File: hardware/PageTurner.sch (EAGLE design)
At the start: 11 parts

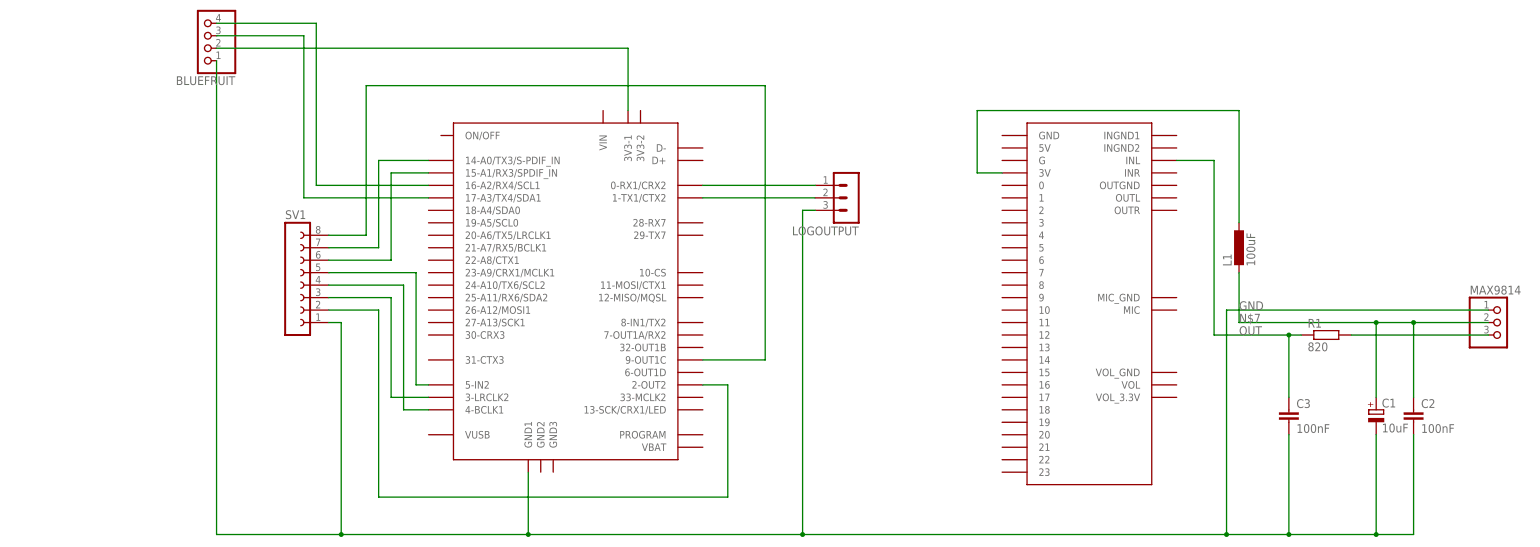
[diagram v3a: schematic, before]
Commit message: trained new model and made python programm not crashing if teensy connection breaks
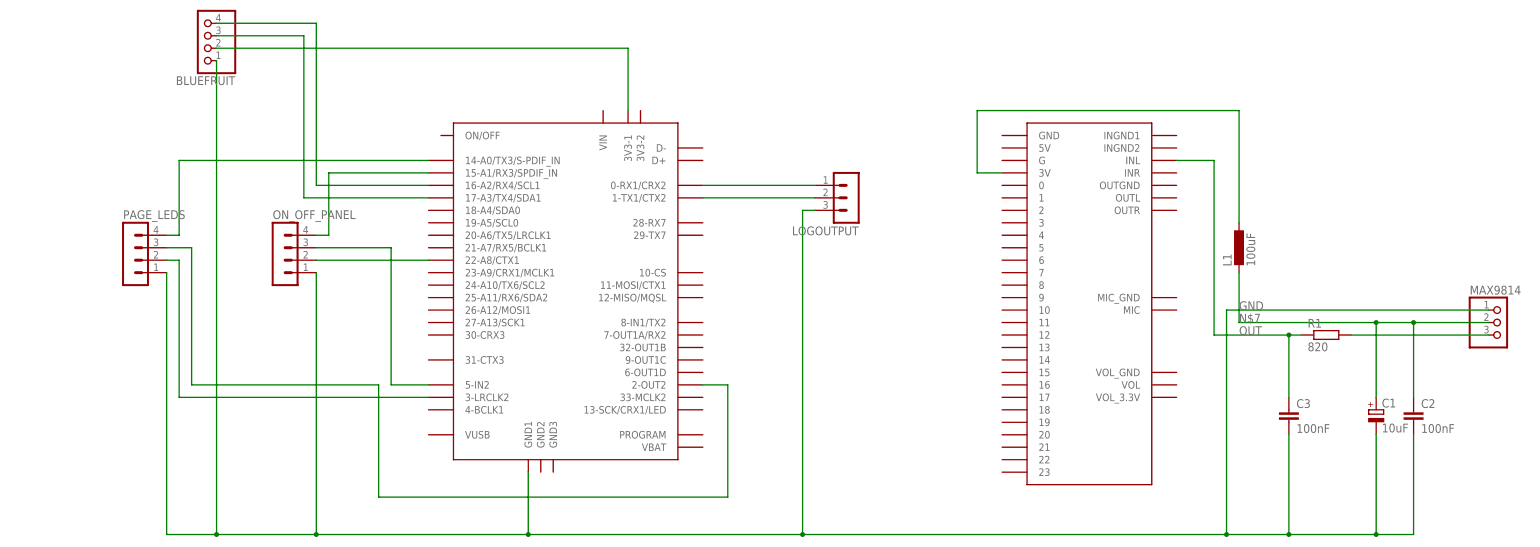
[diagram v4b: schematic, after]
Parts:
- removed SV1: (no value), con-lsta:FE08-1
- added ON_OFF_PANEL, PAGE_LEDS: (no value), con-lstb:MA04-1
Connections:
- net N$10 renamed LOG_TX
- net N$8 renamed LOG_RX
- removed net N$11: SV1.5, U$1.5-IN2
- removed net N$12: SV1.6, U$1.15-A1/RX3/SPDIF_IN
- removed net N$9: SV1.4, U$1.4-BCLK1
- new net N$8: PAGE_LEDS.2, U$1.3-LRCLK2
- net GND: now also ON_OFF_PANEL.1, PAGE_LEDS.1; no longer SV1.1
- net N$1: now also PAGE_LEDS.3; no longer SV1.2
- net N$2: now also PAGE_LEDS.4, U$1.14-A0/TX3/S-PDIF_IN; no longer SV1.7
- net N$3: now also ON_OFF_PANEL.4, U$1.15-A1/RX3/SPDIF_IN; no longer SV1.8, U$1.9-OUT1C
- net N$5: now also ON_OFF_PANEL.3, U$1.5-IN2; no longer U$1.14-A0/TX3/S-PDIF_IN
- net N$6: now also ON_OFF_PANEL.2, U$1.22-A8/CTX1; no longer SV1.3, U$1.3-LRCLK2
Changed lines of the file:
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@@
 <part name="MAX9814" library="pinhead" library_urn="urn:adsk.eagle:library:325" deviceset="PINHD-1X3" device="" package3d_urn="urn:adsk.eagle:package:22458/2"/>
 <part name="BLUEFRUIT" library="pinhead" library_urn="urn:adsk.eagle:library:325" deviceset="PINHD-1X4" device="" package3d_urn="urn:adsk.eagle:package:22407/2"/>
-<part name="SV1" library="con-lsta" library_urn="urn:adsk.eagle:library:161" deviceset="FE08-1" device="" package3d_urn="urn:adsk.eagle:package:8194/1"/>
 <part name="R1" library="rcl" library_urn="urn:adsk.eagle:library:334" deviceset="R-EU_" device="0207/7" package3d_urn="urn:adsk.eagle:package:23493/2" value="820"/>
 <part name="C1" library="rcl" library_urn="urn:adsk.eagle:library:334" deviceset="CPOL-EU" device="E2-4" package3d_urn="urn:adsk.eagle:package:23347/1" value="10uF"/>
@@
 <part name="L1" library="rcl" library_urn="urn:adsk.eagle:library:334" deviceset="L-EU" device="0207/5V" package3d_urn="urn:adsk.eagle:package:23502/1" value="100uF"/>
 <part name="C3" library="rcl" library_urn="urn:adsk.eagle:library:334" deviceset="C-EU" device="025-040X050" package3d_urn="urn:adsk.eagle:package:23634/1" value="100nF"/>
+<part name="PAGE_LEDS" library="con-lstb" library_urn="urn:adsk.eagle:library:162" deviceset="MA04-1" device="" package3d_urn="urn:adsk.eagle:package:8337/1"/>
+<part name="ON_OFF_PANEL" library="con-lstb" library_urn="urn:adsk.eagle:library:162" deviceset="MA04-1" device="" package3d_urn="urn:adsk.eagle:package:8337/1"/>
 </parts>
 <sheets>
@@
 <attribute name="VALUE" x="-11.43" y="109.22" size="1.778" layer="96" rot="R180"/>
 </instance>
-<instance part="SV1" gate="G$1" x="0" y="50.8" smashed="yes">
-<attribute name="VALUE" x="-1.27" y="38.1" size="1.778" layer="96"/>
-<attribute name="NAME" x="-1.27" y="64.262" size="1.778" layer="95"/>
-</instance>
 <instance part="R1" gate="G$1" x="210.82" y="40.64" smashed="yes">
 <attribute name="NAME" x="207.01" y="42.1386" size="1.778" layer="95"/>
@@
 <attribute name="NAME" x="204.724" y="25.781" size="1.778" layer="95"/>
 <attribute name="VALUE" x="204.724" y="20.701" size="1.778" layer="96"/>
+</instance>
+<instance part="PAGE_LEDS" gate="1" x="-33.02" y="58.42" smashed="yes">
+<attribute name="VALUE" x="-34.29" y="48.26" size="1.778" layer="96"/>
+<attribute name="NAME" x="-34.29" y="64.262" size="1.778" layer="95"/>
+</instance>
+<instance part="ON_OFF_PANEL" gate="1" x="-2.54" y="58.42" smashed="yes">
+<attribute name="VALUE" x="-3.81" y="48.26" size="1.778" layer="96"/>
+<attribute name="NAME" x="-3.81" y="64.262" size="1.778" layer="95"/>
 </instance>
 </instances>
@@
 </busses>
 <nets>
-<net name="N$9" class="0">
-<segment>
-<pinref part="SV1" gate="G$1" pin="4"/>
-<wire x1="7.62" y1="50.8" x2="22.86" y2="50.8" width="0.1524" layer="91"/>
-<wire x1="22.86" y1="50.8" x2="22.86" y2="25.4" width="0.1524" layer="91"/>
-<pinref part="U$1" gate="G$1" pin="4-BCLK1"/>
-<wire x1="22.86" y1="25.4" x2="27.94" y2="25.4" width="0.1524" layer="91"/>
-</segment>
-</net>
-<net name="N$8" class="0">
+<net name="LOG_RX" class="0">
 <segment>
 <pinref part="U$1" gate="G$1" pin="0-RX1/CRX2"/>
@@
 </segment>
 </net>
-<net name="N$10" class="0">
+<net name="LOG_TX" class="0">
 <segment>
 <pinref part="U$1" gate="G$1" pin="1-TX1/CTX2"/>
@@
 <wire x1="88.9" y1="30.48" x2="88.9" y2="7.62" width="0.1524" layer="91"/>
 <wire x1="88.9" y1="7.62" x2="17.78" y2="7.62" width="0.1524" layer="91"/>
-<wire x1="17.78" y1="7.62" x2="17.78" y2="45.72" width="0.1524" layer="91"/>
-<pinref part="SV1" gate="G$1" pin="2"/>
-<wire x1="17.78" y1="45.72" x2="7.62" y2="45.72" width="0.1524" layer="91"/>
+<wire x1="17.78" y1="7.62" x2="17.78" y2="30.48" width="0.1524" layer="91"/>
+<pinref part="PAGE_LEDS" gate="1" pin="3"/>
+<wire x1="-25.4" y1="58.42" x2="-20.32" y2="58.42" width="0.1524" layer="91"/>
+<wire x1="-20.32" y1="58.42" x2="-20.32" y2="30.48" width="0.1524" layer="91"/>
+<wire x1="-20.32" y1="30.48" x2="17.78" y2="30.48" width="0.1524" layer="91"/>
 </segment>
 </net>
@@
 <wire x1="190.5" y1="45.72" x2="190.5" y2="0" width="0.1524" layer="91"/>
 <pinref part="U$1" gate="G$1" pin="GND1"/>
-<wire x1="-15.24" y1="0" x2="10.16" y2="0" width="0.1524" layer="91"/>
-<wire x1="10.16" y1="0" x2="48.26" y2="0" width="0.1524" layer="91"/>
+<wire x1="-15.24" y1="0" x2="5.08" y2="0" width="0.1524" layer="91"/>
+<wire x1="5.08" y1="0" x2="48.26" y2="0" width="0.1524" layer="91"/>
 <wire x1="48.26" y1="0" x2="48.26" y2="12.7" width="0.1524" layer="91"/>
 <pinref part="LOGOUTPUT" gate="G$1" pin="3"/>
@@
 <pinref part="BLUEFRUIT" gate="A" pin="1"/>
 <wire x1="-15.24" y1="96.52" x2="-15.24" y2="0" width="0.1524" layer="91"/>
-<pinref part="SV1" gate="G$1" pin="1"/>
-<wire x1="7.62" y1="43.18" x2="10.16" y2="43.18" width="0.1524" layer="91"/>
-<wire x1="10.16" y1="43.18" x2="10.16" y2="0" width="0.1524" layer="91"/>
-<junction x="10.16" y="0"/>
 <pinref part="C1" gate="G$1" pin="-"/>
 <wire x1="220.98" y1="20.32" x2="220.98" y2="0" width="0.1524" layer="91"/>
@@
 <wire x1="203.2" y1="20.32" x2="203.2" y2="0" width="0.1524" layer="91"/>
 <junction x="203.2" y="0"/>
+<pinref part="PAGE_LEDS" gate="1" pin="1"/>
+<wire x1="-25.4" y1="53.34" x2="-25.4" y2="0" width="0.1524" layer="91"/>
+<wire x1="-25.4" y1="0" x2="-15.24" y2="0" width="0.1524" layer="91"/>
+<junction x="-15.24" y="0"/>
+<pinref part="ON_OFF_PANEL" gate="1" pin="1"/>
+<wire x1="5.08" y1="53.34" x2="5.08" y2="0" width="0.1524" layer="91"/>
+<junction x="5.08" y="0"/>
 </segment>
 </net>
@@
 </segment>
 </net>
-<net name="N$3" class="0">
-<segment>
-<pinref part="U$1" gate="G$1" pin="9-OUT1C"/>
-<wire x1="96.52" y1="35.56" x2="83.82" y2="35.56" width="0.1524" layer="91"/>
-<pinref part="SV1" gate="G$1" pin="8"/>
-<wire x1="7.62" y1="60.96" x2="15.24" y2="60.96" width="0.1524" layer="91"/>
-<wire x1="15.24" y1="60.96" x2="15.24" y2="91.44" width="0.1524" layer="91"/>
-<wire x1="15.24" y1="91.44" x2="96.52" y2="91.44" width="0.1524" layer="91"/>
-<wire x1="96.52" y1="91.44" x2="96.52" y2="35.56" width="0.1524" layer="91"/>
-</segment>
-</net>
 <net name="BLE_TX" class="0">
 <segment>
@@
 </segment>
 </net>
-<net name="N$6" class="0">
-<segment>
-<pinref part="SV1" gate="G$1" pin="3"/>
-<wire x1="7.62" y1="48.26" x2="20.32" y2="48.26" width="0.1524" layer="91"/>
-<wire x1="20.32" y1="48.26" x2="20.32" y2="27.94" width="0.1524" layer="91"/>
-<pinref part="U$1" gate="G$1" pin="3-LRCLK2"/>
-<wire x1="27.94" y1="27.94" x2="20.32" y2="27.94" width="0.1524" layer="91"/>
-</segment>
-</net>
-<net name="N$11" class="0">
-<segment>
-<pinref part="SV1" gate="G$1" pin="5"/>
-<wire x1="7.62" y1="53.34" x2="25.4" y2="53.34" width="0.1524" layer="91"/>
-<pinref part="U$1" gate="G$1" pin="5-IN2"/>
-<wire x1="27.94" y1="30.48" x2="25.4" y2="30.48" width="0.1524" layer="91"/>
-<wire x1="25.4" y1="30.48" x2="25.4" y2="53.34" width="0.1524" layer="91"/>
-</segment>
-</net>
-<net name="N$12" class="0">
-<segment>
-<pinref part="U$1" gate="G$1" pin="15-A1/RX3/SPDIF_IN"/>
-<wire x1="27.94" y1="73.66" x2="20.32" y2="73.66" width="0.1524" layer="91"/>
-<wire x1="20.32" y1="55.88" x2="20.32" y2="73.66" width="0.1524" layer="91"/>
-<pinref part="SV1" gate="G$1" pin="6"/>
-<wire x1="7.62" y1="55.88" x2="20.32" y2="55.88" width="0.1524" layer="91"/>
-</segment>
-</net>
-<net name="N$5" class="0">
+<net name="N$2" class="0">
 <segment>
 <pinref part="U$1" gate="G$1" pin="14-A0/TX3/S-PDIF_IN"/>
-<wire x1="27.94" y1="76.2" x2="17.78" y2="76.2" width="0.1524" layer="91"/>
-<wire x1="17.78" y1="76.2" x2="17.78" y2="58.42" width="0.1524" layer="91"/>
-</segment>
-</net>
-<net name="N$2" class="0">
-<segment>
-<pinref part="SV1" gate="G$1" pin="7"/>
-<wire x1="7.62" y1="58.42" x2="17.78" y2="58.42" width="0.1524" layer="91"/>
+<pinref part="PAGE_LEDS" gate="1" pin="4"/>
+<wire x1="-25.4" y1="60.96" x2="-22.86" y2="60.96" width="0.1524" layer="91"/>
+<wire x1="-22.86" y1="60.96" x2="-22.86" y2="76.2" width="0.1524" layer="91"/>
+<wire x1="-22.86" y1="76.2" x2="27.94" y2="76.2" width="0.1524" layer="91"/>
 </segment>
 </net>
@@
 </segment>
 </net>
+<net name="N$8" class="0">
+<segment>
+<pinref part="PAGE_LEDS" gate="1" pin="2"/>
+<wire x1="-25.4" y1="55.88" x2="-22.86" y2="55.88" width="0.1524" layer="91"/>
+<pinref part="U$1" gate="G$1" pin="3-LRCLK2"/>
+<wire x1="-22.86" y1="55.88" x2="-22.86" y2="27.94" width="0.1524" layer="91"/>
+<wire x1="-22.86" y1="27.94" x2="27.94" y2="27.94" width="0.1524" layer="91"/>
+</segment>
+</net>
+<net name="N$3" class="0">
+<segment>
+<pinref part="ON_OFF_PANEL" gate="1" pin="4"/>
+<wire x1="5.08" y1="60.96" x2="7.62" y2="60.96" width="0.1524" layer="91"/>
+<wire x1="7.62" y1="60.96" x2="7.62" y2="73.66" width="0.1524" layer="91"/>
+<pinref part="U$1" gate="G$1" pin="15-A1/RX3/SPDIF_IN"/>
+<wire x1="7.62" y1="73.66" x2="27.94" y2="73.66" width="0.1524" layer="91"/>
+</segment>
+</net>
+<net name="N$5" class="0">
+<segment>
+<pinref part="ON_OFF_PANEL" gate="1" pin="3"/>
+<wire x1="5.08" y1="58.42" x2="20.32" y2="58.42" width="0.1524" layer="91"/>
+<wire x1="20.32" y1="58.42" x2="20.32" y2="30.48" width="0.1524" layer="91"/>
+<pinref part="U$1" gate="G$1" pin="5-IN2"/>
+<wire x1="20.32" y1="30.48" x2="27.94" y2="30.48" width="0.1524" layer="91"/>
+</segment>
+</net>
+<net name="N$6" class="0">
+<segment>
+<pinref part="ON_OFF_PANEL" gate="1" pin="2"/>
+<pinref part="U$1" gate="G$1" pin="22-A8/CTX1"/>
+<wire x1="5.08" y1="55.88" x2="27.94" y2="55.88" width="0.1524" layer="91"/>
+</segment>
+</net>
